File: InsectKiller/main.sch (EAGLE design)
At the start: 28 parts, among them IC3 NE555N, Q1 BCF29SMD, Q2 IRF530, Q3 BCX71SMD

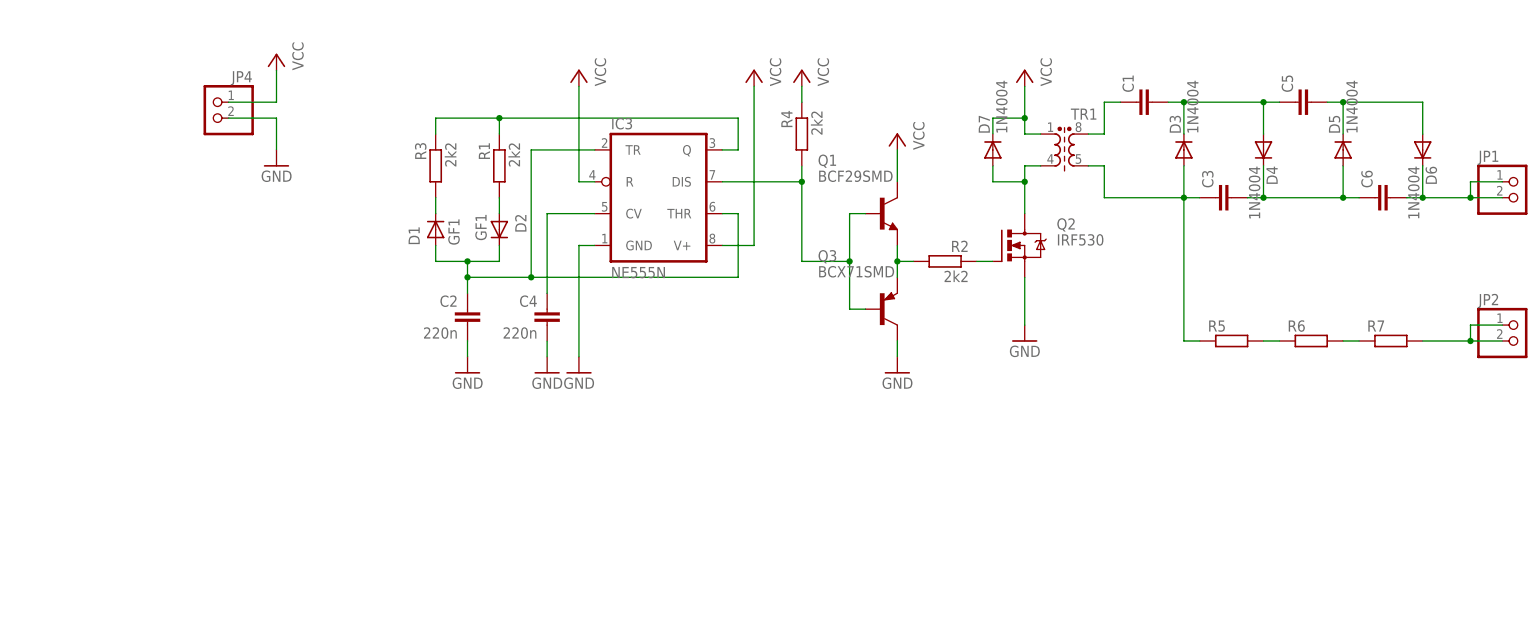
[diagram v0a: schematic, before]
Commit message: Fixed element values.
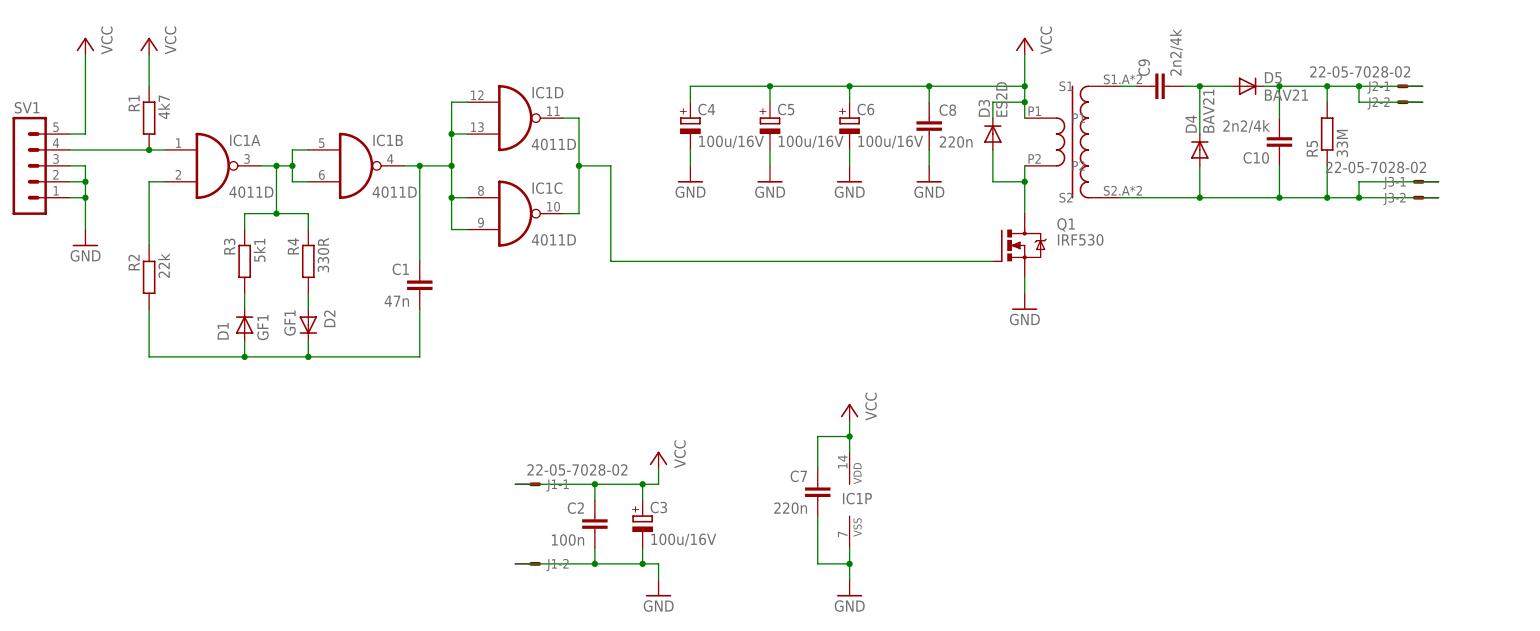
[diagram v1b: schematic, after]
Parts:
- removed D6, D7: 1N4004, diode:1N4004
- removed IC3: NE555N, linear:NE555N
- removed JP1, JP2, JP4: (no value), pinhead:PINHD-1X2
- removed Q2: IRF530, transistor-power:IRF530
- removed Q3: BCX71SMD, transistor-pnp:BCX71SMD
- removed R6, R7: (no value), resistor:R-EU_0207/10
- removed TR1: (no value), inductor-neosid:SMR6-2W
- added 11: CCFL_INVERTER_COIL, ccfl_inverter_coil:CCFL_INVERTER_COIL
- added C10: 2n2/4k, resistor:C-EU075-042X103
- added C7, C8: 220n, resistor:C-EUC0805
- added C9: 2n2/4k, rcl:C-EU075-042X103
- added IC1: 4011D, 40xx:4011D
- added J1, J2, J3: 22-05-7028-02, con-molex:22-05-7028-02
- added SV1: (no value), con-lstb:MA05-1
- C1: value (none) -> 47n; device resistor:C-EU050-024X044 -> resistor:C-EU025-025X050
- C2: value 220n -> 100n
- C3, C6: value (none) -> 100u/16V; device resistor:C-EU050-024X044 -> rcl:CPOL-EU153CLV-0505
- C4: value 220n -> 100u/16V; device resistor:C-EUC0805 -> rcl:CPOL-EU153CLV-0505
- C5: value (none) -> 100u/16V; device resistor:C-EU050-024X044 -> resistor:CPOL-EU153CLV-0505
- D3: value 1N4004 -> ES2D; device diode:1N4004 -> diode:ES2D
- D4, D5: value 1N4004 -> BAV21; device diode:1N4004 -> diode:BAV21
- Q1: value BCF29SMD -> IRF530; device transistor-npn:BCF29SMD -> transistor-power:IRF530
- R1: value 2k2 -> 4k7
- R2: value 2k2 -> 22k
- R3: value 2k2 -> 5k1
- R4: value 2k2 -> 330R
- R5: value (none) -> 33M
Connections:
- removed net N$12: C1.2, C5.1, D3.C, D4.A
- removed net N$13: R5.2, R6.1
- removed net N$14: C3.2, C6.1, D4.C, D5.A
- removed net N$15: C5.2, D5.C, D6.A
- removed net N$16: C6.2, D6.C, JP1.1, JP1.2
- removed net N$17: JP2.1, JP2.2, R7.2
- removed net N$18: R6.2, R7.1
- removed net N$8: C2.1, D1.A, D2.C, IC3.THR, IC3.TR
- new net N$22: IC1A.O, IC1B.I0, IC1B.I1, R3.1, R4.1
- new net N$23: C1.2, D1.A, D2.C, R2.2
- new net N$25: D2.A, R4.2
- net GND: now also C3.-, C4.-, C5.-, C6.-, C7.2, C8.2, IC1P.VSS, J1-2.S, Q1.S, SV1.1, SV1.2, SV1.3; no longer C4.2, IC3.GND, JP4.2, Q2.S, Q3.C
- net N$1: now also IC1A.I1, R2.1; no longer Q1.E, Q3.E, R2.2
- net N$10: now also C10.2, D5.C, J2-1.S, J2-2.S, R5.2; no longer D2.A, R1.2
- net N$11: now also 11.S2, C10.1, D4.A, J3-1.S, J3-2.S; no longer C3.1, D3.A, TR1.5
- net N$2: now also IC1A.I0, R1.2, SV1.4; no longer Q2.G, R2.1
- net N$3: now also 11.P2, D3.A, Q1.D; no longer D7.A, Q2.D, TR1.4
- net N$4: now also IC1C.O, IC1D.O, Q1.G; no longer IC3.DIS, Q1.B, Q3.B, R4.2
- net N$5: now also C1.1, IC1B.O, IC1C.I0, IC1C.I1, IC1D.I0, IC1D.I1; no longer IC3.Q, R1.1, R3.1
- net N$6: now also 11.S1, C9.1; no longer C4.1, IC3.CV
- net N$7: now also C9.2, D4.C, D5.A; no longer C1.1, TR1.8
- net VCC: now also 11.P1, C2.1, C3.+, C4.+, C5.+, C6.+, C7.1, C8.1, D3.C, IC1P.VDD, J1-1.S, R1.1, SV1.5; no longer D7.C, IC3.R, IC3.V+, JP4.1, Q1.C, R4.1, TR1.1
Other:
- moved on the sheet: C1, C2, D1, D2, D4, D5, R1, R2, R3, R4, R5

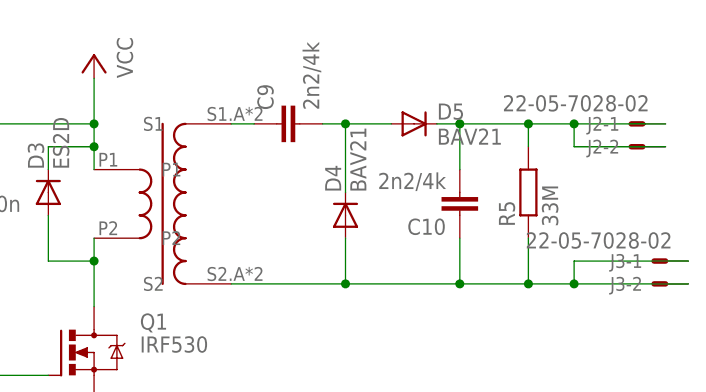
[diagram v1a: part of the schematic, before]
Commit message: Fixed capacitor value.
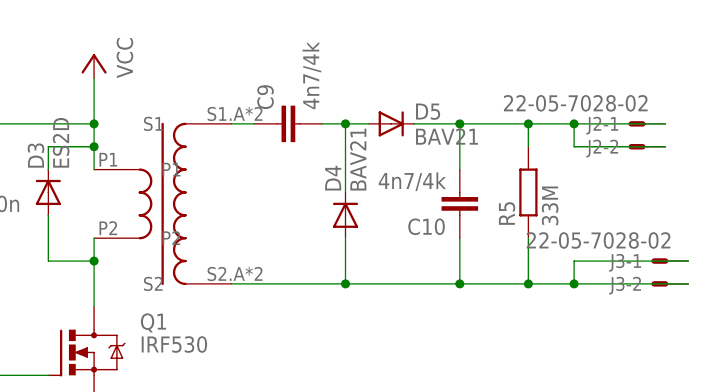
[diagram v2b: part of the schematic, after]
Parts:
- C10, C9: value 2n2/4k -> 4n7/4k
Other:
- moved on the sheet: D5
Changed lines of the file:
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@@
 <layer number="97" name="Info" color="7" fill="1" visible="yes" active="yes"/>
 <layer number="98" name="Guide" color="6" fill="1" visible="yes" active="yes"/>
-<layer number="99" name="SpiceOrder" color="5" fill="1" visible="yes" active="yes"/>
+<layer number="99" name="SpiceOrder" color="5" fill="1" visible="no" active="yes"/>
 <layer number="100" name="help" color="7" fill="1" visible="yes" active="yes"/>
 <layer number="101" name="DOC" color="7" fill="1" visible="yes" active="yes"/>
@@
 <part name="C7" library="resistor" deviceset="C-EU" device="C0805" value="220n"/>
 <part name="Q1" library="transistor-power" deviceset="IRF530" device=""/>
-<part name="C9" library="rcl" deviceset="C-EU" device="075-042X103" value="2n2/4k"/>
+<part name="C9" library="rcl" deviceset="C-EU" device="075-042X103" value="4n7/4k"/>
 <part name="R5" library="resistor" deviceset="R-EU_" device="0207/10" value="33M"/>
 <part name="D3" library="diode" deviceset="ES2D" device=""/>
@@
 <part name="C8" library="resistor" deviceset="C-EU" device="C0805" value="220n"/>
 <part name="D5" library="diode" deviceset="BAV21" device=""/>
-<part name="C10" library="resistor" deviceset="C-EU" device="075-042X103" value="2n2/4k"/>
+<part name="C10" library="resistor" deviceset="C-EU" device="075-042X103" value="4n7/4k"/>
 <part name="D4" library="diode" deviceset="BAV21" device=""/>
 <part name="GND7" library="supply1" deviceset="GND" device=""/>
@@
 <instance part="GND6" gate="1" x="22.86" y="-10.16" rot="MR0"/>
 <instance part="C8" gate="G$1" x="35.56" y="66.04"/>
-<instance part="D5" gate="1" x="86.36" y="71.12"/>
+<instance part="D5" gate="1" x="83.82" y="71.12"/>
 <instance part="C10" gate="G$1" x="91.44" y="60.96" rot="R180"/>
 <instance part="D4" gate="1" x="78.74" y="60.96" rot="R90"/>
@@
 <wire x1="76.2" y1="71.12" x2="78.74" y2="71.12" width="0.1524" layer="91"/>
 <pinref part="D5" gate="1" pin="A"/>
-<wire x1="78.74" y1="71.12" x2="83.82" y2="71.12" width="0.1524" layer="91"/>
+<wire x1="78.74" y1="71.12" x2="81.28" y2="71.12" width="0.1524" layer="91"/>
 <junction x="78.74" y="71.12"/>
 <pinref part="D4" gate="1" pin="C"/>
@@
 <pinref part="C10" gate="G$1" pin="2"/>
 <wire x1="91.44" y1="71.12" x2="91.44" y2="66.04" width="0.1524" layer="91"/>
-<wire x1="88.9" y1="71.12" x2="91.44" y2="71.12" width="0.1524" layer="91"/>
+<wire x1="86.36" y1="71.12" x2="91.44" y2="71.12" width="0.1524" layer="91"/>
 <wire x1="104.14" y1="68.58" x2="114.3" y2="68.58" width="0.1524" layer="91"/>
 <wire x1="114.3" y1="71.12" x2="104.14" y2="71.12" width="0.1524" layer="91"/>
